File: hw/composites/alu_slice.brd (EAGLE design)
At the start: 50 x 50 mm, 7 parts, among them CON2 GENERIC-2X10

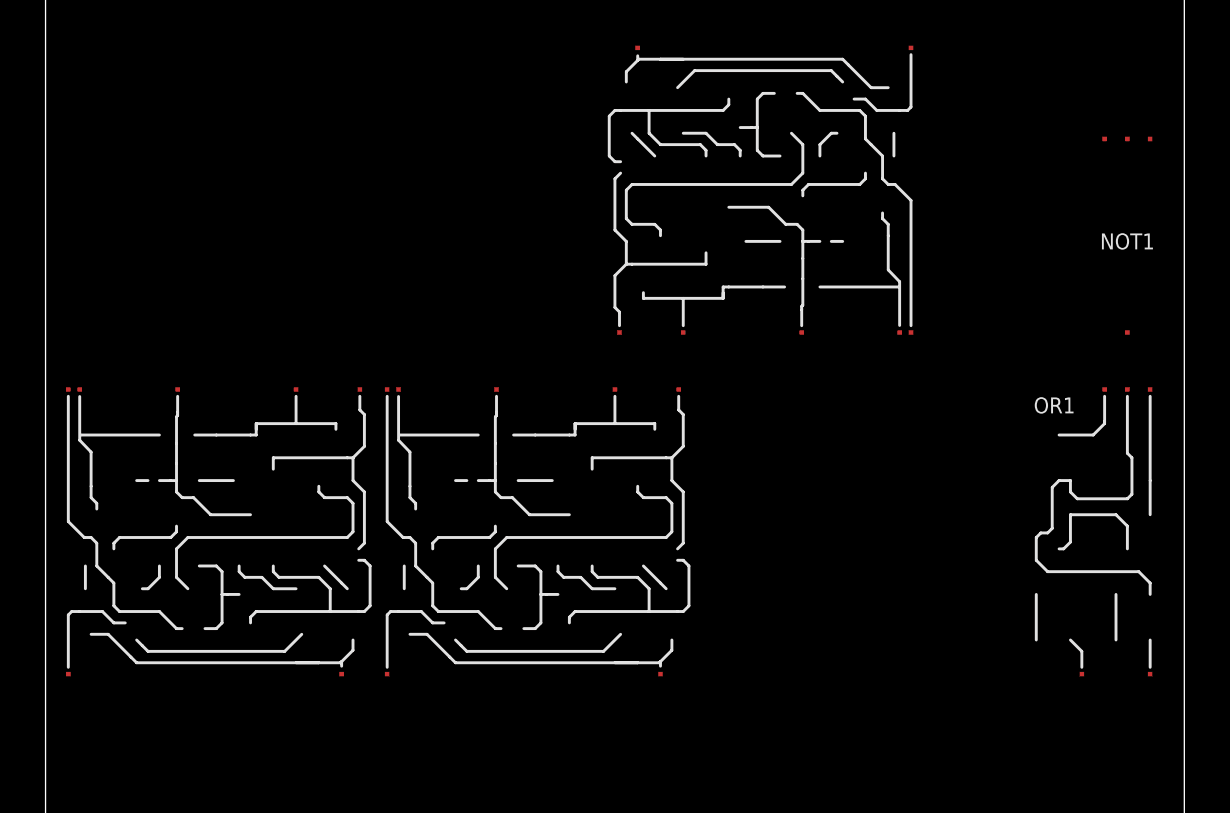
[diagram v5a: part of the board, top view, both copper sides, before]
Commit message: Simplified circuit
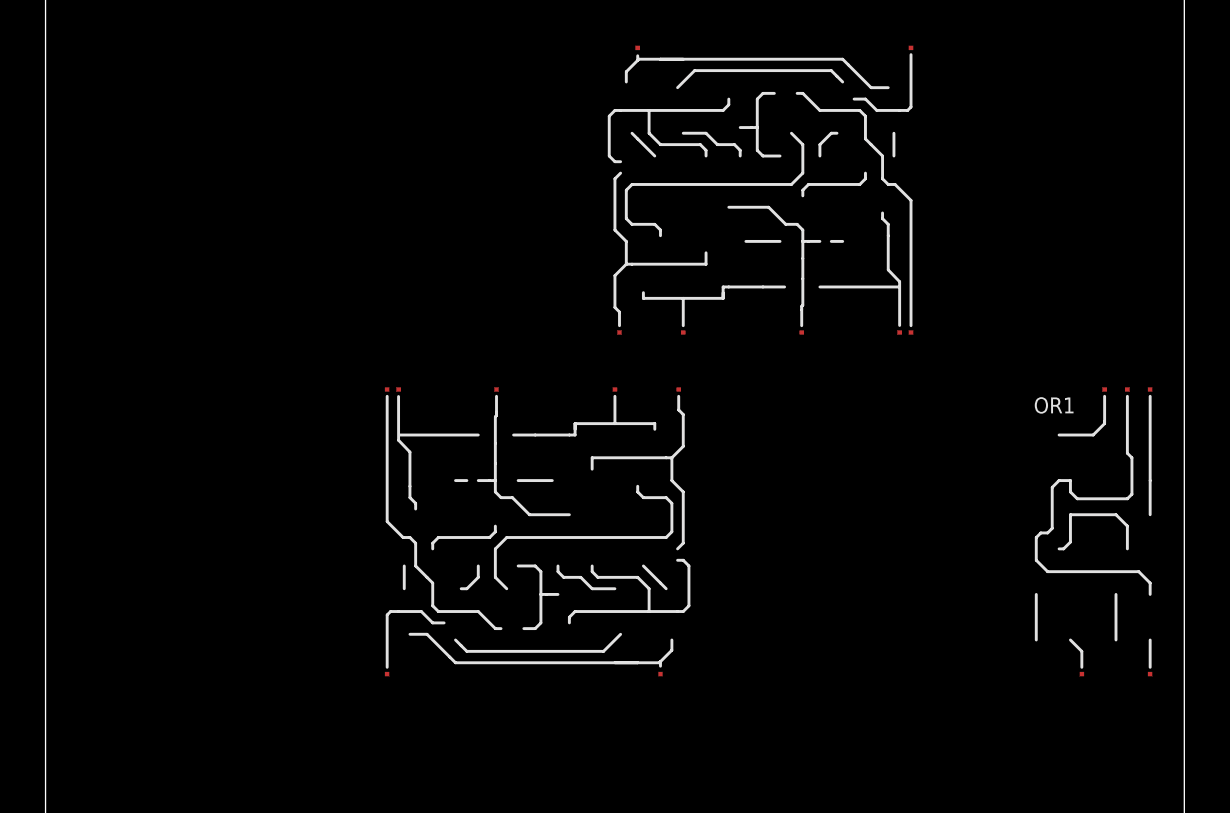
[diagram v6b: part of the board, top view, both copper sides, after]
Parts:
- removed NOT1: NOTVERTICAL, p.peter-gator:NOT-VERTICAL
- removed XOR1: XOR, p.peter-gator:XOR
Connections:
- removed net B_INT: XOR1.XOR, XOR2.B
- removed net INVERT: XOR1.B
- removed net N$6: NOT1.A, OR1.B, XOR2.AND
- removed net NAND: NOT1.NOT, SEL2.I8
- new net AND: OR1.B, SEL2.I8, XOR2.AND
- net +5V: no longer NOT1._VP, XOR1._VP
- net B: now also XOR2.B; no longer XOR1.A
- net GND: no longer NOT1._VN, XOR1._VN
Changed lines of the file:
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@@
 </autorouter>
 <elements>
-<element name="XOR1" library="p.peter-gator" package="XOR" value="XOR" x="0.5" y="19.5"/>
 <element name="XOR2" library="p.peter-gator" package="XOR" value="XOR" x="38.5" y="47" rot="R180"/>
 <element name="XOR3" library="p.peter-gator" package="XOR" value="XOR" x="14.5" y="19.5"/>
-<element name="NOT1" library="p.peter-gator" package="NOT-VERTICAL" value="NOTVERTICAL" x="45.5" y="34.5"/>
 <element name="OR1" library="p.peter-gator" package="OR" value="OR" x="42.5" y="19.5"/>
 <element name="SEL2" library="p.peter-gator" package="SELECTOR-8_BIT-NOMUX" value="8_BIT_SELECT" x="10" y="5"/>
@@
 </signal>
 <signal name="+5V">
-<contactref element="XOR1" pad="_VP"/>
 <contactref element="XOR2" pad="_VP"/>
-<contactref element="NOT1" pad="_VP"/>
 <contactref element="XOR3" pad="_VP"/>
 <contactref element="OR1" pad="_VP"/>
 <contactref element="SEL2" pad="_VP"/>
 <contactref element="CON2" pad="19"/>
-<wire x1="48.5" y1="32" x2="48.5" y2="43" width="0" layer="19" extent="1-1"/>
 <wire x1="37.5" y1="34.5" x2="48.5" y2="32" width="0" layer="19" extent="1-1"/>
 <wire x1="15.5" y1="32" x2="37.5" y2="34.5" width="0" layer="19" extent="1-1"/>
-<wire x1="1.5" y1="32" x2="15.5" y2="32" width="0" layer="19" extent="1-1"/>
 <wire x1="48" y1="5" x2="48.5" y2="32" width="0" layer="19" extent="1-1"/>
 <wire x1="39.93" y1="1.27" x2="48" y2="5" width="0" layer="19" extent="1-16"/>
 </signal>
 <signal name="GND">
-<contactref element="XOR1" pad="_VN"/>
 <contactref element="XOR2" pad="_VN"/>
-<contactref element="NOT1" pad="_VN"/>
 <contactref element="XOR3" pad="_VN"/>
 <contactref element="OR1" pad="_VN"/>
 <contactref element="SEL2" pad="_VN"/>
 <contactref element="CON2" pad="20"/>
-<wire x1="47.5" y1="32" x2="47.5" y2="43" width="0" layer="19" extent="1-1"/>
 <wire x1="27.8" y1="32" x2="47.5" y2="32" width="0" layer="19" extent="1-1"/>
 <wire x1="25.2" y1="34.5" x2="27.8" y2="32" width="0" layer="19" extent="1-1"/>
-<wire x1="13.8" y1="32" x2="25.2" y2="34.5" width="0" layer="19" extent="1-1"/>
 <wire x1="46" y1="5" x2="47.5" y2="32" width="0" layer="19" extent="1-1"/>
 <wire x1="39.93" y1="1.27" x2="46" y2="5" width="0" layer="19" extent="1-1"/>
@@
 <wire x1="39.8" y1="5" x2="33.2" y2="34.5" width="0" layer="19" extent="1-1"/>
 </signal>
-<signal name="NAND">
-<contactref element="NOT1" pad="NOT"/>
-<contactref element="SEL2" pad="I8"/>
-<wire x1="44.2" y1="5" x2="46.5" y2="43" width="0" layer="19" extent="1-1"/>
-</signal>
-<signal name="B_INT">
-<contactref element="XOR1" pad="XOR"/>
-<contactref element="XOR2" pad="B"/>
-<wire x1="11" y1="32" x2="38" y2="47" width="0" layer="19" extent="1-1"/>
-</signal>
 <signal name="B">
-<contactref element="XOR1" pad="A"/>
 <contactref element="SEL2" pad="I2"/>
 <contactref element="CON2" pad="3"/>
-<wire x1="17.8" y1="5" x2="13" y2="19.5" width="0" layer="19" extent="1-1"/>
+<contactref element="XOR2" pad="B"/>
+<wire x1="17.8" y1="5" x2="38" y2="47" width="0" layer="19" extent="1-1"/>
 <wire x1="19.61" y1="1.27" x2="17.8" y2="5" width="0" layer="19" extent="1-16"/>
-</signal>
-<signal name="INVERT">
-<contactref element="XOR1" pad="B"/>
 </signal>
 <signal name="LEFT_IN">
@@
 <contactref element="CON2" pad="9"/>
 </signal>
-<signal name="N$6">
+<signal name="AND">
 <contactref element="OR1" pad="B"/>
 <contactref element="XOR2" pad="AND"/>
-<contactref element="NOT1" pad="A"/>
-<wire x1="38" y1="34.5" x2="47.5" y2="34.5" width="0" layer="19" extent="1-1"/>
-<wire x1="48.5" y1="19.5" x2="47.5" y2="34.5" width="0" layer="19" extent="1-1"/>
+<contactref element="SEL2" pad="I8"/>
+<wire x1="48.5" y1="19.5" x2="38" y2="34.5" width="0" layer="19" extent="1-1"/>
+<wire x1="44.2" y1="5" x2="48.5" y2="19.5" width="0" layer="19" extent="1-1"/>
 </signal>
 <signal name="N$8">

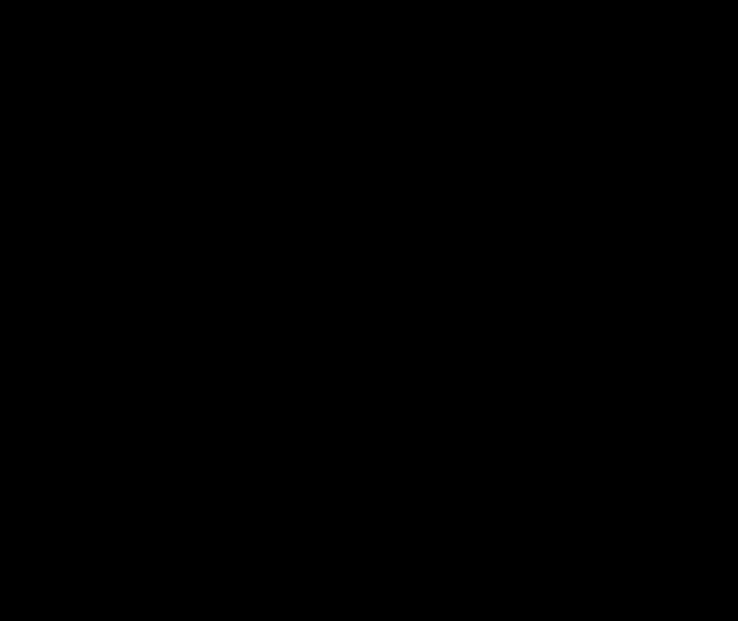
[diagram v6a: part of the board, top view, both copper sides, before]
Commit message: Added inversion of output
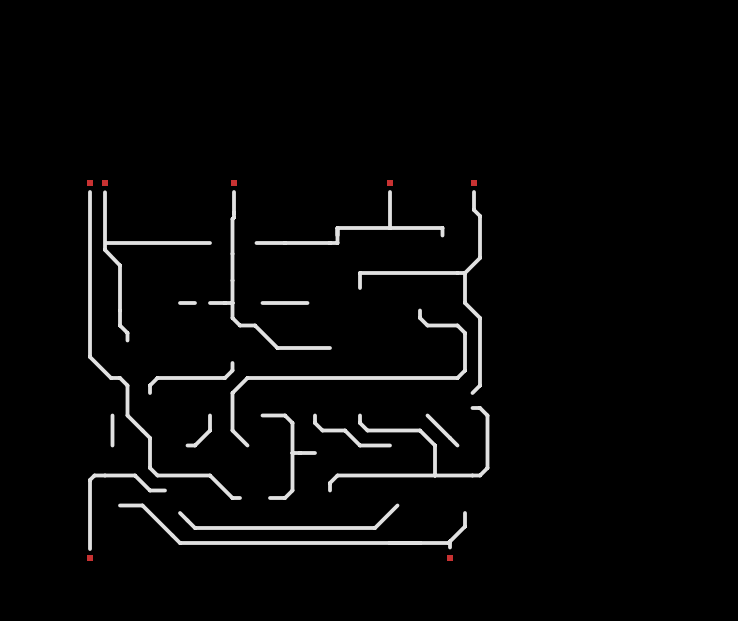
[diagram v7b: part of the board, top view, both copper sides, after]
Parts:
- added XOR1: XOR, p.peter-gator:XOR
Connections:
- removed net EQUAL_IN: CON2.13
- removed net EQUAL_OUT: CON2.17
- removed net OVERFLOW: CON2.5
- removed net RIGHT_IN: CON2.1
- removed net RIGHT_OUT: CON2.9
- new net INVERT_OUT: CON2.7, XOR1.B
- new net N$1: SEL2.OUT, XOR1.A
- new net NC: CON2.10, CON2.11, CON2.12, CON2.13, CON2.14, CON2.16, CON2.18, CON2.8, CON2.9
- net +5V: now also XOR1._VP
- net A: now also CON2.1; no longer CON2.10
- net CARRY_IN: now also CON2.5
- net CARRY_OUT: now also CON2.17; no longer CON2.11
- net GND: now also XOR1._VN
- net LEFT_IN: no longer CON2.7
- net RESULT: now also XOR1.XOR; no longer SEL2.OUT
- net S_ADD: now also CON2.6; no longer CON2.12
- net S_AND: now also CON2.4; no longer CON2.18
- net S_CMP: no longer CON2.6
- net S_ID: now also CON2.2; no longer CON2.8
- net S_LOAD: no longer CON2.4
- net S_OR: no longer CON2.16
- net S_SHIFT: no longer CON2.2
- net S_XOR: no longer CON2.14
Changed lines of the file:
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@@
 <element name="SEL2" library="p.peter-gator" package="SELECTOR-8_BIT-NOMUX" value="8_BIT_SELECT" x="10" y="5"/>
 <element name="CON2" library="p.peter-connectors" package="PINHEADER-100MIL-2X10-EDGE" value="GENERIC-2X10" x="28.5" y="0"/>
+<element name="XOR1" library="p.peter-gator" package="XOR" value="XOR" x="0.5" y="-20"/>
 </elements>
 <signals>
@@
 <contactref element="XOR2" pad="A"/>
 <contactref element="SEL2" pad="I4"/>
-<contactref element="CON2" pad="10"/>
+<contactref element="CON2" pad="1"/>
 <wire x1="26.6" y1="5" x2="26" y2="47" width="0" layer="19" extent="1-1"/>
-<wire x1="27.23" y1="1.27" x2="26.6" y2="5" width="0" layer="19" extent="1-1"/>
+<wire x1="17.07" y1="1.27" x2="26.6" y2="5" width="0" layer="19" extent="1-16"/>
 </signal>
 <signal name="XOR">
@@
 <signal name="CARRY_IN">
 <contactref element="XOR3" pad="A"/>
+<contactref element="CON2" pad="5"/>
+<wire x1="22.15" y1="1.27" x2="27" y2="19.5" width="0" layer="19" extent="1-16"/>
 </signal>
 <signal name="SUM">
@@
 </signal>
 <signal name="CARRY_OUT">
-<contactref element="CON2" pad="11"/>
 <contactref element="OR1" pad="OR"/>
-<wire x1="29.77" y1="1.27" x2="46.5" y2="32" width="0" layer="19" extent="1-16"/>
+<contactref element="CON2" pad="17"/>
+<wire x1="37.39" y1="1.27" x2="46.5" y2="32" width="0" layer="19" extent="1-16"/>
 </signal>
 <signal name="+5V">
@@
 <contactref element="SEL2" pad="_VP"/>
 <contactref element="CON2" pad="19"/>
+<contactref element="XOR1" pad="_VP"/>
 <wire x1="37.5" y1="34.5" x2="48.5" y2="32" width="0" layer="19" extent="1-1"/>
 <wire x1="15.5" y1="32" x2="37.5" y2="34.5" width="0" layer="19" extent="1-1"/>
 <wire x1="48" y1="5" x2="48.5" y2="32" width="0" layer="19" extent="1-1"/>
 <wire x1="39.93" y1="1.27" x2="48" y2="5" width="0" layer="19" extent="1-16"/>
+<wire x1="1.5" y1="-7.5" x2="39.93" y2="1.27" width="0" layer="19" extent="1-16"/>
 </signal>
 <signal name="GND">
@@
 <contactref element="SEL2" pad="_VN"/>
 <contactref element="CON2" pad="20"/>
+<contactref element="XOR1" pad="_VN"/>
 <wire x1="27.8" y1="32" x2="47.5" y2="32" width="0" layer="19" extent="1-1"/>
 <wire x1="25.2" y1="34.5" x2="27.8" y2="32" width="0" layer="19" extent="1-1"/>
 <wire x1="46" y1="5" x2="47.5" y2="32" width="0" layer="19" extent="1-1"/>
 <wire x1="39.93" y1="1.27" x2="46" y2="5" width="0" layer="19" extent="1-1"/>
+<wire x1="13.8" y1="-7.5" x2="39.93" y2="1.27" width="0" layer="19" extent="1-1"/>
 </signal>
 <signal name="NOR">
@@
 <signal name="LEFT_IN">
 <contactref element="SEL2" pad="I3"/>
-<contactref element="CON2" pad="7"/>
 <contactref element="SEL2" pad="I1"/>
-<wire x1="24.69" y1="1.27" x2="22.2" y2="5" width="0" layer="19" extent="1-16"/>
 <wire x1="13.4" y1="5" x2="22.2" y2="5" width="0" layer="19" extent="1-1"/>
-</signal>
-<signal name="EQUAL_IN">
-<contactref element="CON2" pad="13"/>
-</signal>
-<signal name="EQUAL_OUT">
-<contactref element="CON2" pad="17"/>
-</signal>
-<signal name="RIGHT_IN">
-<contactref element="CON2" pad="1"/>
-</signal>
-<signal name="RIGHT_OUT">
-<contactref element="CON2" pad="9"/>
 </signal>
 <signal name="AND">
@@
 <signal name="S_OR">
 <contactref element="SEL2" pad="S7"/>
-<contactref element="CON2" pad="16"/>
-<wire x1="34.85" y1="1.27" x2="37.6" y2="5" width="0" layer="19" extent="1-1"/>
 </signal>
 <signal name="S_XOR">
 <contactref element="SEL2" pad="S6"/>
-<contactref element="CON2" pad="14"/>
-<wire x1="32.31" y1="1.27" x2="33.2" y2="5" width="0" layer="19" extent="1-1"/>
 </signal>
 <signal name="S_ADD">
 <contactref element="SEL2" pad="S5"/>
-<contactref element="CON2" pad="12"/>
-<wire x1="29.77" y1="1.27" x2="28.8" y2="5" width="0" layer="19" extent="1-1"/>
+<contactref element="CON2" pad="6"/>
+<wire x1="22.15" y1="1.27" x2="28.8" y2="5" width="0" layer="19" extent="1-1"/>
 </signal>
 <signal name="S_CMP">
 <contactref element="SEL2" pad="S3"/>
-<contactref element="CON2" pad="6"/>
-<wire x1="22.15" y1="1.27" x2="20" y2="5" width="0" layer="19" extent="1-1"/>
 </signal>
 <signal name="S_LOAD">
 <contactref element="SEL2" pad="S2"/>
-<contactref element="CON2" pad="4"/>
-<wire x1="19.61" y1="1.27" x2="15.6" y2="5" width="0" layer="19" extent="1-1"/>
 </signal>
 <signal name="S_ID">
 <contactref element="SEL2" pad="S4"/>
-<contactref element="CON2" pad="8"/>
-<wire x1="24.69" y1="1.27" x2="24.4" y2="5" width="0" layer="19" extent="1-1"/>
+<contactref element="CON2" pad="2"/>
+<wire x1="17.07" y1="1.27" x2="24.4" y2="5" width="0" layer="19" extent="1-1"/>
 </signal>
 <signal name="S_AND">
 <contactref element="SEL2" pad="S8"/>
-<contactref element="CON2" pad="18"/>
-<wire x1="37.39" y1="1.27" x2="42" y2="5" width="0" layer="19" extent="1-1"/>
+<contactref element="CON2" pad="4"/>
+<wire x1="19.61" y1="1.27" x2="42" y2="5" width="0" layer="19" extent="1-1"/>
 </signal>
 <signal name="S_SHIFT">
 <contactref element="SEL2" pad="S1"/>
-<contactref element="CON2" pad="2"/>
-<wire x1="11.2" y1="5" x2="17.07" y2="1.27" width="0" layer="19" extent="1-1"/>
-</signal>
-<signal name="OVERFLOW">
-<contactref element="CON2" pad="5"/>
 </signal>
 <signal name="RESULT">
 <contactref element="CON2" pad="15"/>
-<contactref element="SEL2" pad="OUT"/>
-<wire x1="34.85" y1="1.27" x2="47" y2="5" width="0" layer="19" extent="1-16"/>
+<contactref element="XOR1" pad="XOR"/>
+<wire x1="11" y1="-7.5" x2="34.85" y2="1.27" width="0" layer="19" extent="1-16"/>
 </signal>
 <signal name="N$4">
 </signal>
+<signal name="NC">
+<contactref element="CON2" pad="9"/>
+<contactref element="CON2" pad="11"/>
+<contactref element="CON2" pad="13"/>
+<contactref element="CON2" pad="8"/>
+<contactref element="CON2" pad="10"/>
+<contactref element="CON2" pad="12"/>
+<contactref element="CON2" pad="14"/>
+<contactref element="CON2" pad="16"/>
+<contactref element="CON2" pad="18"/>
+<wire x1="34.85" y1="1.27" x2="37.39" y2="1.27" width="0" layer="19" extent="1-1"/>
+<wire x1="32.31" y1="1.27" x2="34.85" y2="1.27" width="0" layer="19" extent="1-16"/>
+<wire x1="32.31" y1="1.27" x2="32.31" y2="1.27" width="0" layer="19" extent="1-16"/>
+<wire x1="29.77" y1="1.27" x2="32.31" y2="1.27" width="0" layer="19" extent="16-16"/>
+<wire x1="29.77" y1="1.27" x2="29.77" y2="1.27" width="0" layer="19" extent="1-16"/>
+<wire x1="27.23" y1="1.27" x2="29.77" y2="1.27" width="0" layer="19" extent="16-16"/>
+<wire x1="27.23" y1="1.27" x2="27.23" y2="1.27" width="0" layer="19" extent="1-16"/>
+<wire x1="24.69" y1="1.27" x2="27.23" y2="1.27" width="0" layer="19" extent="1-16"/>
+</signal>
+<signal name="INVERT_OUT">
+<contactref element="CON2" pad="7"/>
+<contactref element="XOR1" pad="B"/>
+<wire x1="1" y1="-20" x2="24.69" y2="1.27" width="0" layer="19" extent="1-16"/>
+</signal>
+<signal name="N$1">
+<contactref element="SEL2" pad="OUT"/>
+<contactref element="XOR1" pad="A"/>
+<wire x1="13" y1="-20" x2="47" y2="5" width="0" layer="19" extent="1-1"/>
+</signal>
 </signals>
